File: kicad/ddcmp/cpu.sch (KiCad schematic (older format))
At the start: 9 parts, among them J1 UART, J4 TEST, U1 Pico

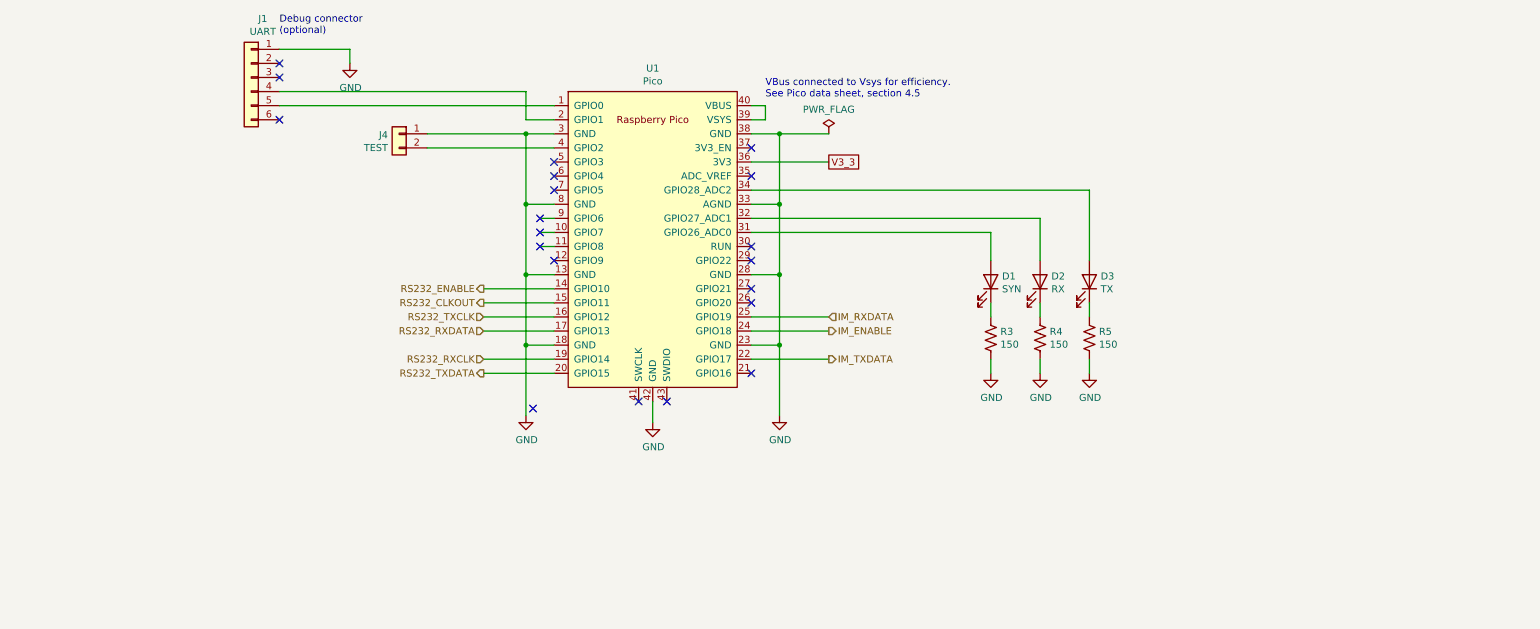
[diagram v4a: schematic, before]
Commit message: Small schematics changes. Rewrite the integral modem receive demodulator state machine.
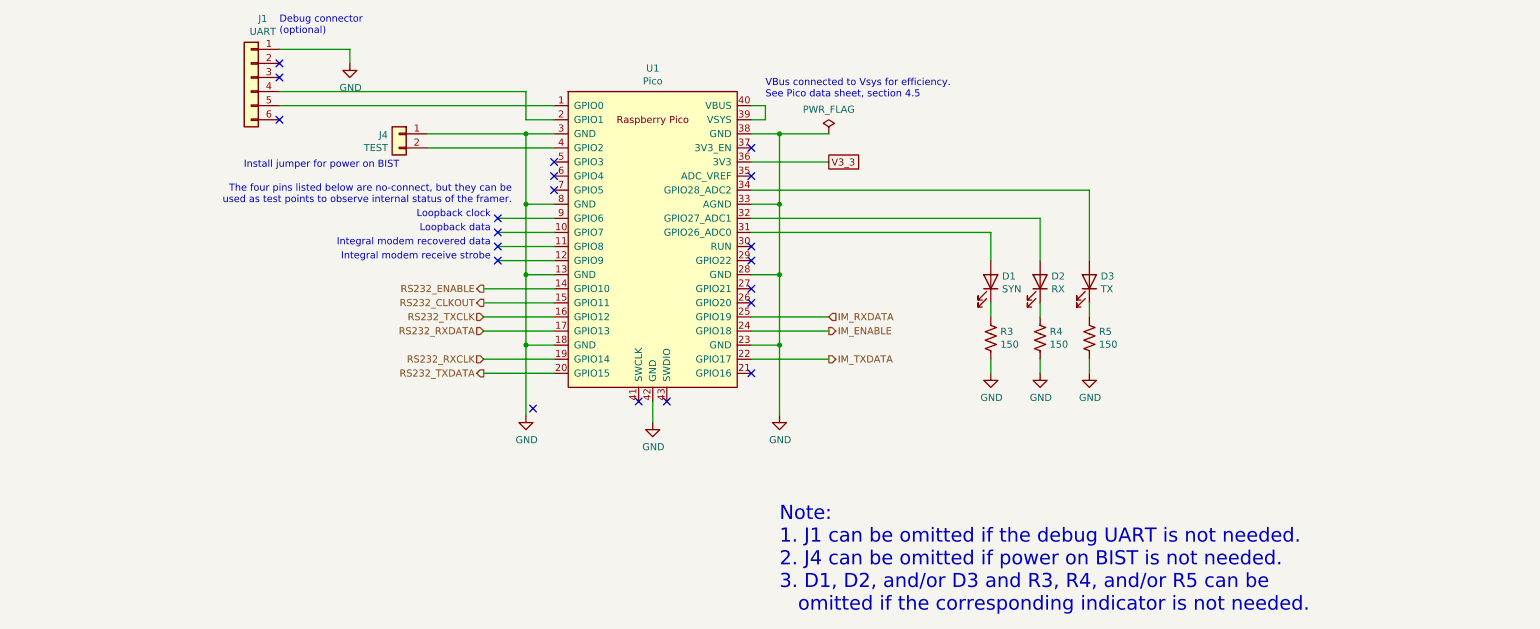
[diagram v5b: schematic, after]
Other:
- note added: "Install jumper for power on BIST"
- note added: "Integral modem receive strobe"
- note added: "Integral modem recovered data"
- note added: "Loopback clock"
- note added: "Loopback data"
- note added: "Note:\n1. J1 can be omitted if the debug UART is not needed.\n2. J4 can be omitted if power on BIST is not needed.\n3. D1, D2, and/or D3 and R3, R4, and/or R5 can be\n omitted if the corresponding indicator is not needed."
- note added: "The four pins listed below are no-connect, but they can be\nused as test points to observe internal status of the framer."
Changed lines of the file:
@@
 F 1 "150" H 8418 4155 50  0000 L CNN
 F 2 "ddcmp_parts:R_Axial_DIN0207_L6.3mm_D2.5mm_P10.16mm_Horizontal" V 8390 4190 50  0001 C CNN
-F 3 "" H 8350 4200 50  0001 C CNN
+F 3 "https://www.yageo.com/upload/media/product/products/datasheet/lr/Yageo_LR_CFR_1.pdf" H 8350 4200 50  0001 C CNN
 F 4 "150QBK-ND" H 8350 4200 50  0001 C CNN "Digikey part"
 F 5 "Yageo" H 8350 4200 50  0001 C CNN "Vendor"
@@
 F 1 "150" H 8768 4155 50  0000 L CNN
 F 2 "ddcmp_parts:R_Axial_DIN0207_L6.3mm_D2.5mm_P10.16mm_Horizontal" V 8740 4190 50  0001 C CNN
-F 3 "" H 8700 4200 50  0001 C CNN
+F 3 "https://www.yageo.com/upload/media/product/products/datasheet/lr/Yageo_LR_CFR_1.pdf" H 8700 4200 50  0001 C CNN
 F 4 "150QBK-ND" H 8700 4200 50  0001 C CNN "Digikey part"
 F 5 "Yageo" H 8700 4200 50  0001 C CNN "Vendor"
@@
 F 1 "150" H 9118 4155 50  0000 L CNN
 F 2 "ddcmp_parts:R_Axial_DIN0207_L6.3mm_D2.5mm_P10.16mm_Horizontal" V 9090 4190 50  0001 C CNN
-F 3 "" H 9050 4200 50  0001 C CNN
+F 3 "https://www.yageo.com/upload/media/product/products/datasheet/lr/Yageo_LR_CFR_1.pdf" H 9050 4200 50  0001 C CNN
 F 4 "150QBK-ND" H 9050 4200 50  0001 C CNN "Digikey part"
 F 5 "Yageo" H 9050 4200 50  0001 C CNN "Vendor"
@@
 Text HLabel 4750 4450 0    50   Output ~ 0
 RS232_TXDATA
-Wire Wire Line
-	5250 3350 5150 3350
-Wire Wire Line
-	5250 3450 5150 3450
-NoConn ~ 5150 3350
-NoConn ~ 5150 3450
 $Comp
 L Connector_Generic:Conn_01x02 J4
@@
 Wire Wire Line
 	9050 3150 9050 3650
-Wire Wire Line
-	5250 3550 5150 3550
-NoConn ~ 5150 3550
-NoConn ~ 5250 3650
 NoConn ~ 5250 3050
 NoConn ~ 5250 2950
@@
 Text Notes 6750 2500 0    50   ~ 0
 VBus connected to Vsys for efficiency.\nSee Pico data sheet, section 4.5
+Wire Wire Line
+	4850 3350 5250 3350
+Wire Wire Line
+	4850 3450 5250 3450
+Wire Wire Line
+	4850 3550 5250 3550
+NoConn ~ 4850 3350
+NoConn ~ 4850 3450
+NoConn ~ 4850 3550
+Text Notes 4800 3350 2    50   ~ 0
+Loopback clock
+Text Notes 4800 3450 2    50   ~ 0
+Loopback data
+Text Notes 4800 3550 2    50   ~ 0
+Integral modem recovered data
+Text Notes 4150 3000 2    50   ~ 0
+Install jumper for power on BIST
+Wire Wire Line
+	5250 3650 4850 3650
+NoConn ~ 4850 3650
+Text Notes 4800 3650 2    50   ~ 0
+Integral modem receive strobe
+Text Notes 4950 3250 2    50   ~ 0
+The four pins listed below are no-connect, but they can be\nused as test points to observe internal status of the framer.
+Text Notes 6850 6150 0    100  ~ 0
+Note:\n1. J1 can be omitted if the debug UART is not needed.\n2. J4 can be omitted if power on BIST is not needed.\n3. D1, D2, and/or D3 and R3, R4, and/or R5 can be\n   omitted if the corresponding indicator is not needed.
 $EndSCHEMATC

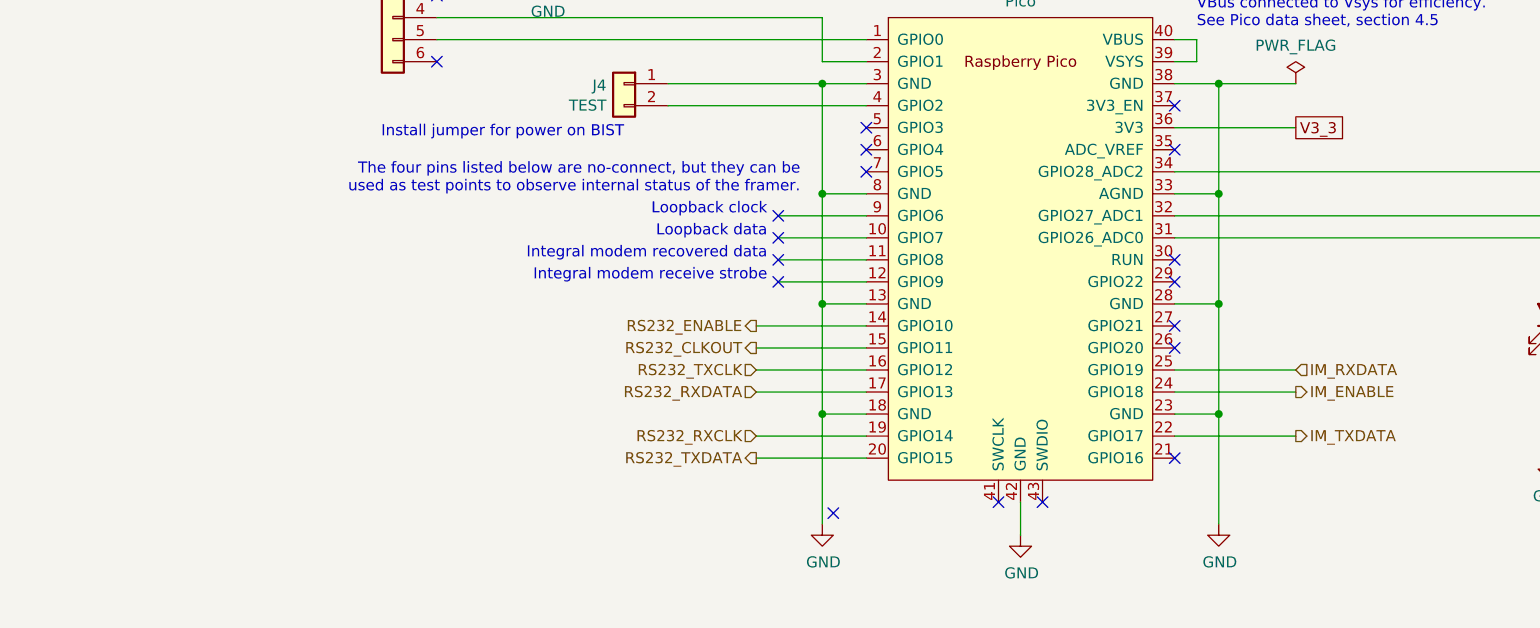
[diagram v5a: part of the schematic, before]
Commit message: 1. Add bit clock monitor and abort frame reception if clock is lost. 2. Make frequency measurement better for integral modem case. 3. New test mode: raw waveform (for integral modem).
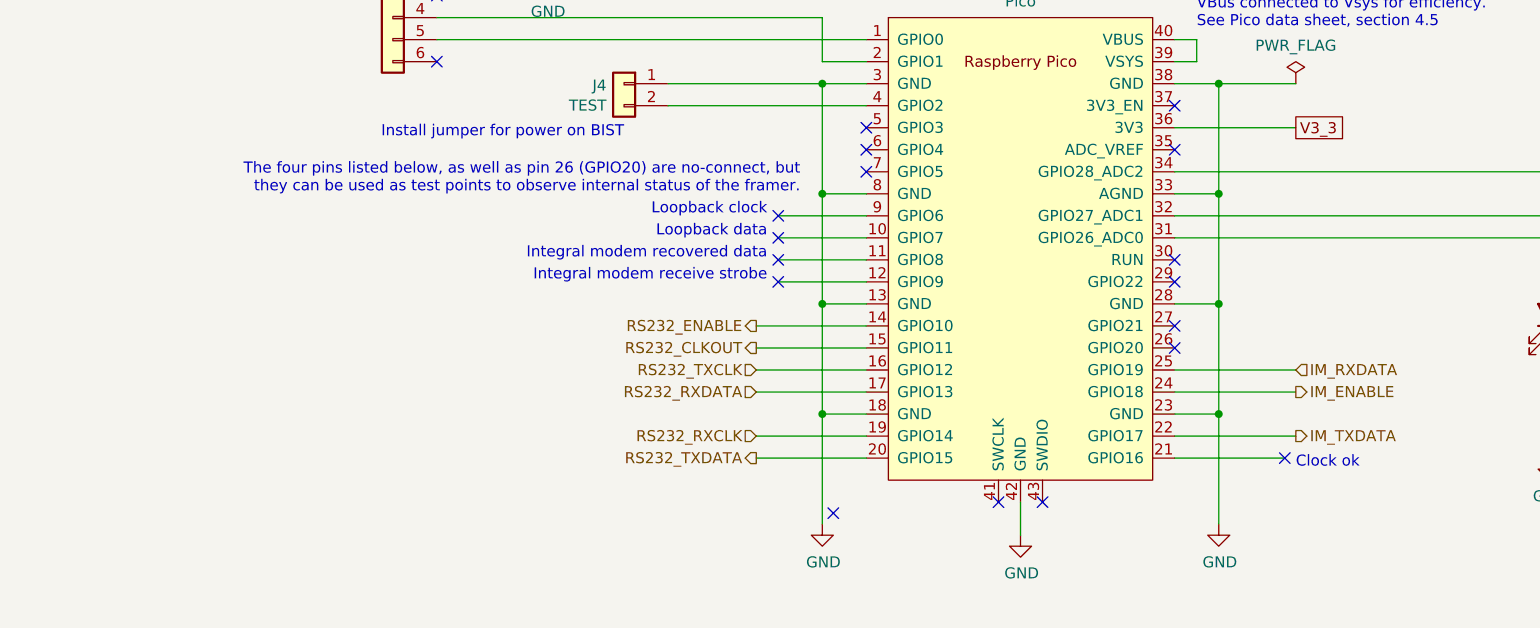
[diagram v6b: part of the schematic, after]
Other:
- note added: "Clock ok"
- note added: "The four pins listed below, as well as pin 26 (GPIO20) are no-connect, but \nthey can be used as test points to observe internal status of the framer."
- note removed: "The four pins listed below are no-connect, but they can be\nused as test points to observe internal status of the framer."
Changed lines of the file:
@@
 NoConn ~ 6650 3650
 NoConn ~ 6650 3850
-NoConn ~ 6650 3950
-NoConn ~ 6650 4450
 Wire Wire Line
 	6650 2750 6850 2750
@@
 Integral modem receive strobe
 Text Notes 4950 3250 2    50   ~ 0
-The four pins listed below are no-connect, but they can be\nused as test points to observe internal status of the framer.
+The four pins listed below, as well as pin 26 (GPIO20) are no-connect, but \nthey can be used as test points to observe internal status of the framer.
 Text Notes 6850 6150 0    100  ~ 0
 Note:\n1. J1 can be omitted if the debug UART is not needed.\n2. J4 can be omitted if power on BIST is not needed.\n3. D1, D2, and/or D3 and R3, R4, and/or R5 can be\n   omitted if the corresponding indicator is not needed.
+Wire Wire Line
+	6650 4450 7150 4450
+NoConn ~ 7150 4450
+Text Notes 7200 4500 0    50   ~ 0
+Clock ok
+NoConn ~ 6650 3950
 $EndSCHEMATC

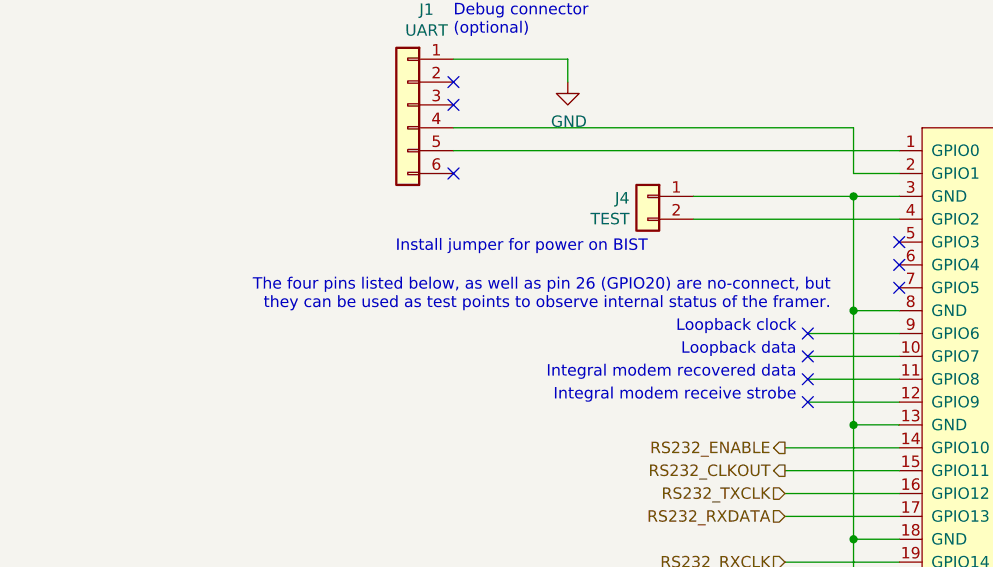
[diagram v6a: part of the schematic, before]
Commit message: Fix description of test point on page 4 of the schematic.
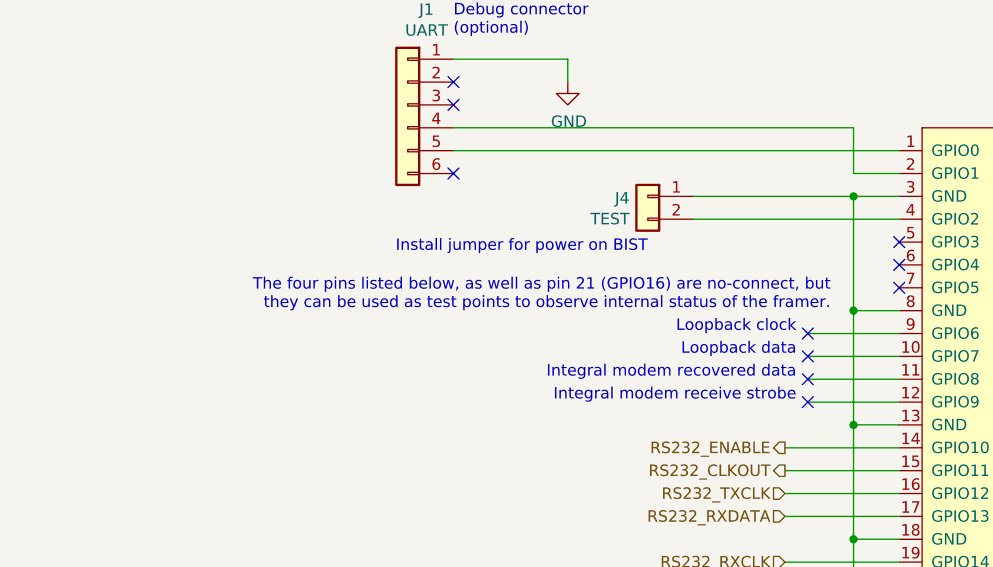
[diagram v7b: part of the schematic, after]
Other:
- note added: "The four pins listed below, as well as pin 21 (GPIO16) are no-connect, but \nthey can be used as test points to observe internal status of the framer."
- note removed: "The four pins listed below, as well as pin 26 (GPIO20) are no-connect, but \nthey can be used as test points to observe internal status of the framer."
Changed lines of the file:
@@
 Integral modem receive strobe
 Text Notes 4950 3250 2    50   ~ 0
-The four pins listed below, as well as pin 26 (GPIO20) are no-connect, but \nthey can be used as test points to observe internal status of the framer.
+The four pins listed below, as well as pin 21 (GPIO16) are no-connect, but \nthey can be used as test points to observe internal status of the framer.
 Text Notes 6850 6150 0    100  ~ 0
 Note:\n1. J1 can be omitted if the debug UART is not needed.\n2. J4 can be omitted if power on BIST is not needed.\n3. D1, D2, and/or D3 and R3, R4, and/or R5 can be\n   omitted if the corresponding indicator is not needed.
